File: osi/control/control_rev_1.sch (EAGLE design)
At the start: 13 parts, among them J1 1X2-3.5MM, J2 1X2-3.5MM

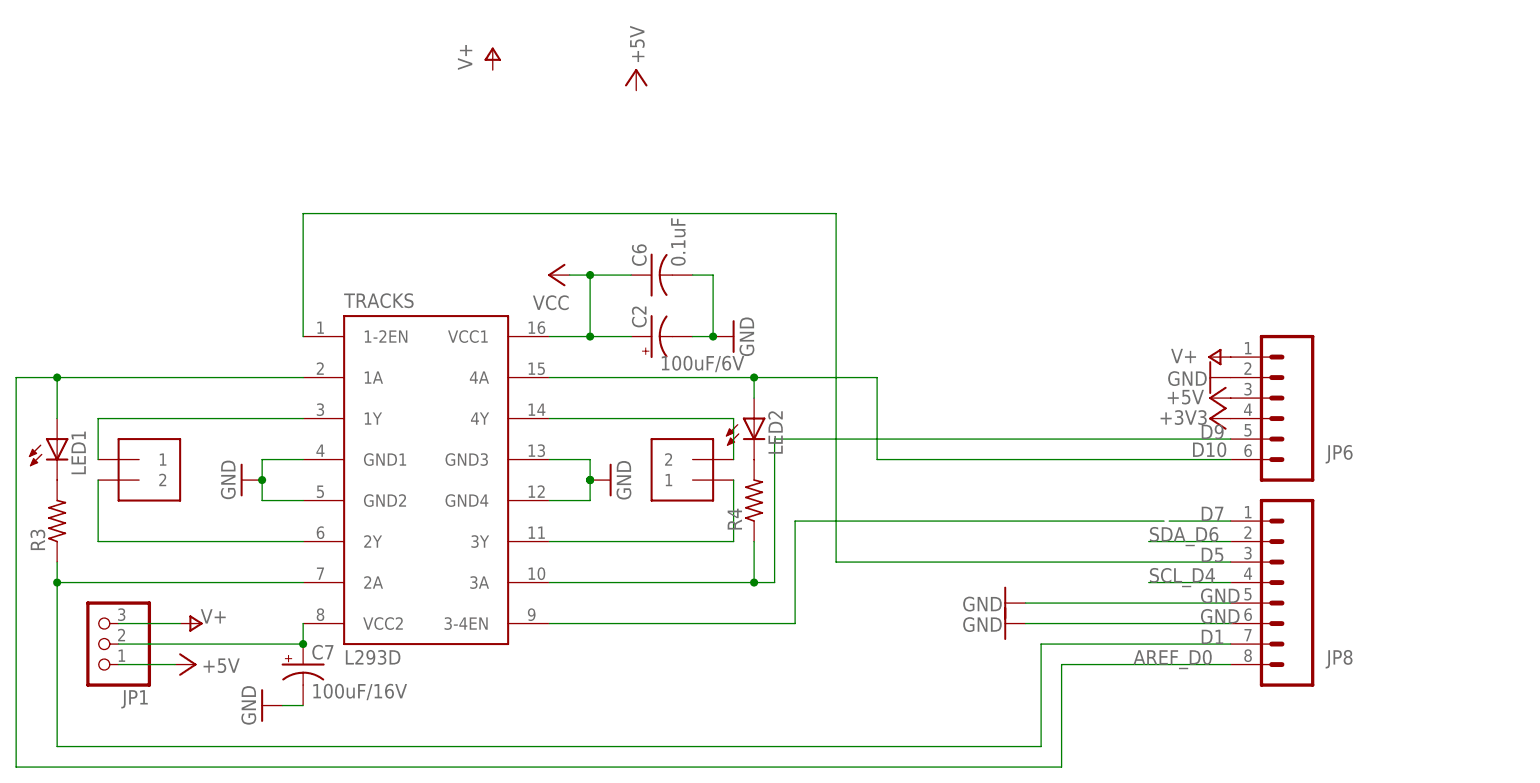
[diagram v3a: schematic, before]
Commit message: D9 -> D8 for INT0
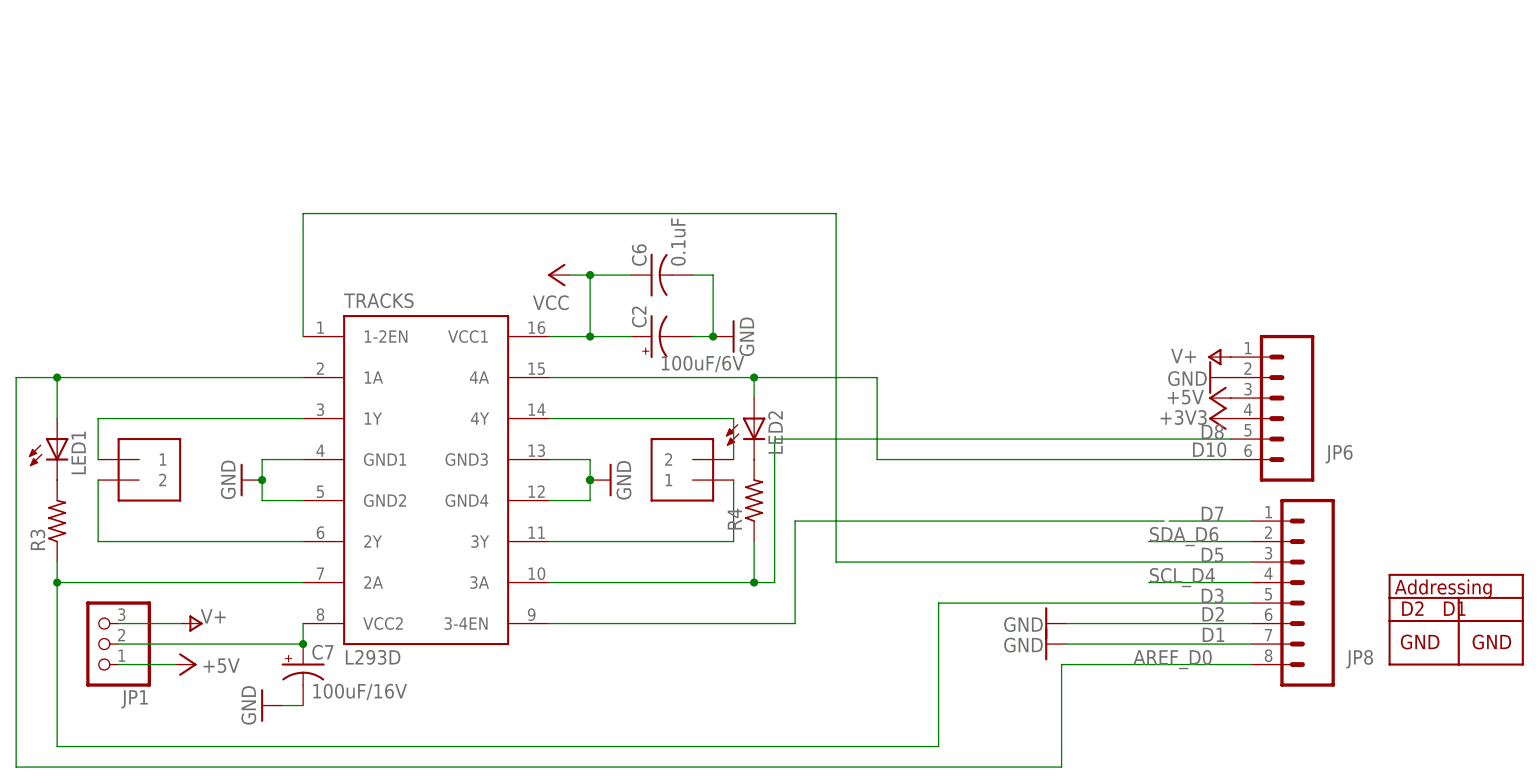
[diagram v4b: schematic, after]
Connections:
- net D9 renamed D8
- new net D2: JP8.6
- new net D3: JP8.5, R3.1, TRACKS.2A
- net D1: no longer R3.1, TRACKS.2A
- net GND: no longer JP8.5, JP8.6
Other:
- moved on the sheet: JP8
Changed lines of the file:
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@@
 <part name="GND5" library="SparkFun" deviceset="GND" device=""/>
 <part name="P+2" library="supply1" deviceset="V+" device=""/>
-<part name="P+6" library="supply1" deviceset="+5V" device=""/>
-<part name="P+7" library="supply1" deviceset="V+" device=""/>
 <part name="+3V4" library="supply1" deviceset="+3V3" device=""/>
 <part name="P+3" library="supply1" deviceset="+5V" device=""/>
@@
 <part name="JP1" library="adafruit_mod" deviceset="PINHD-1X3" device=""/>
 <part name="P+1" library="supply1" deviceset="+5V" device=""/>
+<part name="GND" library="_my-parts" deviceset="ADDRESSING" device="" value="GND"/>
 </parts>
 <sheets>
@@
 <attribute name="VALUE" x="187.071" y="97.536" size="1.778" layer="96" rot="R180"/>
 </instance>
-<instance part="P+6" gate="1" x="117.475" y="132.08" smashed="yes">
-<attribute name="VALUE" x="118.491" y="132.842" size="1.778" layer="96" rot="R90"/>
-</instance>
-<instance part="P+7" gate="1" x="99.695" y="134.62"/>
 <instance part="+3V4" gate="G$1" x="188.595" y="88.9" smashed="yes" rot="R90">
 <attribute name="VALUE" x="188.341" y="89.916" size="1.778" layer="96" rot="R180"/>
@@
 <attribute name="NAME" x="206.375" y="85.598" size="1.778" layer="95" rot="R180"/>
 </instance>
-<instance part="JP8" gate="G$1" x="196.215" y="68.58" smashed="yes" rot="R180">
-<attribute name="VALUE" x="201.295" y="81.28" size="1.778" layer="96" rot="R180"/>
-<attribute name="NAME" x="206.375" y="60.198" size="1.778" layer="95" rot="R180"/>
+<instance part="JP8" gate="G$1" x="198.755" y="68.58" smashed="yes" rot="R180">
+<attribute name="VALUE" x="203.835" y="81.28" size="1.778" layer="96" rot="R180"/>
+<attribute name="NAME" x="208.915" y="60.198" size="1.778" layer="95" rot="R180"/>
 </instance>
 <instance part="FRAME1" gate="G$1" x="0" y="0"/>
@@
 <instance part="J1" gate="G$1" x="55.88" y="81.28"/>
 <instance part="J2" gate="G$1" x="124.46" y="83.82" rot="R180"/>
-<instance part="GND1" gate="1" x="163.195" y="66.04" smashed="yes" rot="R270">
-<attribute name="VALUE" x="157.861" y="65.024" size="1.778" layer="96"/>
-</instance>
-<instance part="GND2" gate="1" x="163.195" y="63.5" smashed="yes" rot="R270">
-<attribute name="VALUE" x="157.861" y="62.484" size="1.778" layer="96"/>
+<instance part="GND1" gate="1" x="168.275" y="63.5" smashed="yes" rot="R270">
+<attribute name="VALUE" x="162.941" y="62.484" size="1.778" layer="96"/>
+</instance>
+<instance part="GND2" gate="1" x="168.275" y="60.96" smashed="yes" rot="R270">
+<attribute name="VALUE" x="162.941" y="59.944" size="1.778" layer="96"/>
 </instance>
 <instance part="LED1" gate="G$1" x="45.72" y="86.36"/>
@@
 <attribute name="VALUE" x="63.627" y="57.404" size="1.778" layer="96"/>
 </instance>
+<instance part="GND" gate="G$1" x="210.82" y="58.42"/>
 </instances>
 <busses>
@@
 <junction x="111.76" y="81.28"/>
 </segment>
-<segment>
-<pinref part="JP8" gate="G$1" pin="5"/>
+</net>
+<net name="D3" class="0">
+<segment>
 <label x="187.325" y="66.04" size="1.778" layer="95"/>
-<wire x1="191.135" y1="66.04" x2="165.735" y2="66.04" width="0.1524" layer="91"/>
-<pinref part="GND1" gate="1" pin="GND"/>
-</segment>
-<segment>
-<pinref part="JP8" gate="G$1" pin="6"/>
-<label x="187.325" y="63.5" size="1.778" layer="95"/>
-<wire x1="191.135" y1="63.5" x2="165.735" y2="63.5" width="0.1524" layer="91"/>
-<pinref part="GND2" gate="1" pin="GND"/>
-</segment>
-</net>
-<net name="D1" class="0">
-<segment>
-<pinref part="JP8" gate="G$1" pin="7"/>
-<label x="187.325" y="60.96" size="1.778" layer="95"/>
 <pinref part="TRACKS" gate="G$1" pin="2A"/>
 <wire x1="76.2" y1="68.58" x2="45.72" y2="68.58" width="0.1524" layer="91"/>
 <wire x1="45.72" y1="68.58" x2="45.72" y2="48.26" width="0.1524" layer="91"/>
-<wire x1="45.72" y1="48.26" x2="167.64" y2="48.26" width="0.1524" layer="91"/>
-<wire x1="167.64" y1="48.26" x2="167.64" y2="60.96" width="0.1524" layer="91"/>
-<wire x1="167.64" y1="60.96" x2="191.135" y2="60.96" width="0.1524" layer="91"/>
+<wire x1="45.72" y1="48.26" x2="154.94" y2="48.26" width="0.1524" layer="91"/>
 <pinref part="R3" gate="G$1" pin="1"/>
 <wire x1="45.72" y1="71.12" x2="45.72" y2="68.58" width="0.1524" layer="91"/>
 <junction x="45.72" y="68.58"/>
+<wire x1="193.675" y1="66.04" x2="154.94" y2="66.04" width="0.1524" layer="91"/>
+<wire x1="154.94" y1="66.04" x2="154.94" y2="48.26" width="0.1524" layer="91"/>
+<pinref part="JP8" gate="G$1" pin="5"/>
 </segment>
 </net>
@@
 <wire x1="40.64" y1="45.72" x2="170.18" y2="45.72" width="0.1524" layer="91"/>
 <wire x1="170.18" y1="45.72" x2="170.18" y2="58.42" width="0.1524" layer="91"/>
-<wire x1="170.18" y1="58.42" x2="191.135" y2="58.42" width="0.1524" layer="91"/>
+<wire x1="170.18" y1="58.42" x2="193.675" y2="58.42" width="0.1524" layer="91"/>
 <pinref part="LED1" gate="G$1" pin="A"/>
 <wire x1="45.72" y1="88.9" x2="45.72" y2="93.98" width="0.1524" layer="91"/>
@@
 <net name="SDA_D6" class="0">
 <segment>
-<wire x1="180.975" y1="73.66" x2="191.135" y2="73.66" width="0.1524" layer="91"/>
+<wire x1="180.975" y1="73.66" x2="193.675" y2="73.66" width="0.1524" layer="91"/>
 <pinref part="JP8" gate="G$1" pin="2"/>
 <label x="180.975" y="73.66" size="1.778" layer="95"/>
@@
 <pinref part="JP8" gate="G$1" pin="3"/>
 <label x="187.325" y="71.12" size="1.778" layer="95"/>
-<wire x1="191.135" y1="71.12" x2="142.24" y2="71.12" width="0.1524" layer="91"/>
+<wire x1="193.675" y1="71.12" x2="142.24" y2="71.12" width="0.1524" layer="91"/>
 <wire x1="142.24" y1="71.12" x2="142.24" y2="114.3" width="0.1524" layer="91"/>
 <pinref part="TRACKS" gate="G$1" pin="1-2EN"/>
@@
 <net name="SCL_D4" class="0">
 <segment>
-<wire x1="180.975" y1="68.58" x2="191.135" y2="68.58" width="0.1524" layer="91"/>
+<wire x1="180.975" y1="68.58" x2="193.675" y2="68.58" width="0.1524" layer="91"/>
 <pinref part="JP8" gate="G$1" pin="4"/>
 <label x="180.975" y="68.58" size="1.778" layer="95"/>
 </segment>
 </net>
-<net name="D9" class="0">
+<net name="D8" class="0">
 <segment>
 <pinref part="JP6" gate="G$1" pin="5"/>
@@
 <net name="D7" class="0">
 <segment>
-<wire x1="183.515" y1="76.2" x2="191.135" y2="76.2" width="0.1524" layer="91"/>
+<wire x1="183.515" y1="76.2" x2="193.675" y2="76.2" width="0.1524" layer="91"/>
 <pinref part="JP8" gate="G$1" pin="1"/>
 <label x="187.325" y="76.2" size="1.778" layer="95"/>
@@
 </segment>
 </net>
+<net name="D1" class="0">
+<segment>
+<pinref part="JP8" gate="G$1" pin="7"/>
+<pinref part="GND2" gate="1" pin="GND"/>
+<wire x1="170.815" y1="60.96" x2="193.675" y2="60.96" width="0.1524" layer="91"/>
+<label x="187.452" y="61.214" size="1.778" layer="95"/>
+</segment>
+</net>
+<net name="D2" class="0">
+<segment>
+<pinref part="JP8" gate="G$1" pin="6"/>
+<label x="190.5" y="65.532" size="1.778" layer="95" rot="R180"/>
+<pinref part="GND1" gate="1" pin="GND"/>
+<wire x1="170.815" y1="63.5" x2="193.675" y2="63.5" width="0.1524" layer="91"/>
+</segment>
+</net>
 </nets>
 </sheet>
@@
 </schematic>
 </drawing>
+<compatibility>
+<note version="6.3" minversion="6.2.2" severity="warning">
+Since Version 6.2.2 text objects can contain more than one line,
+which will not be processed correctly with this version.
+</note>
+</compatibility>
 </eagle>
